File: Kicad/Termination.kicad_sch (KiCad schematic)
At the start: 27 parts, among them J1 Conn_02x25_Odd_Even, J5 5787170-5, SW1 219-8MST, U10 SN74F244DB, U8 DS21S07A, U9 DS21S07A

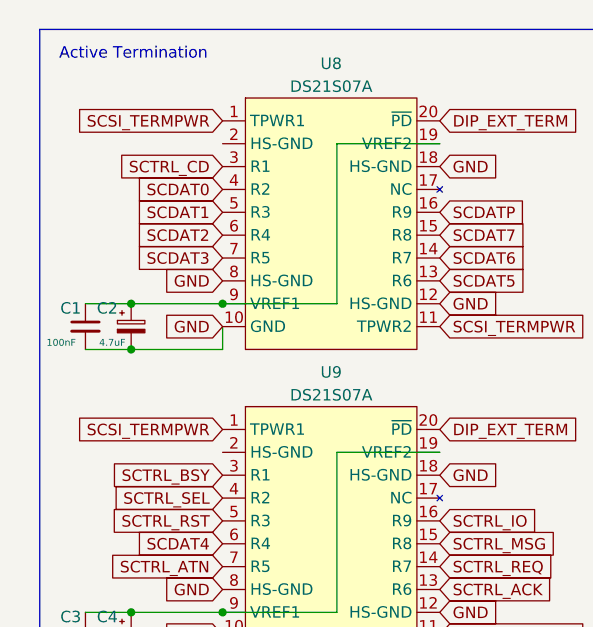
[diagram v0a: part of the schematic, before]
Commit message: Fix HS_GND connection on pin2 of the scsi terminators
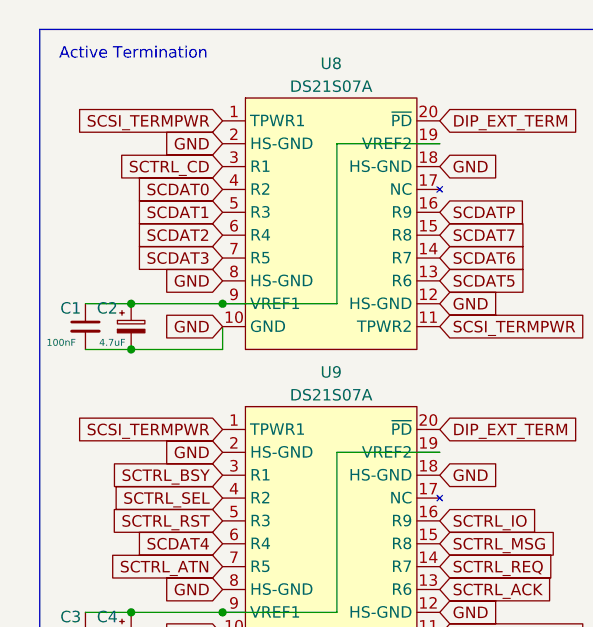
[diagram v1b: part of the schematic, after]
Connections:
- net GND: now also U8.2 (HS-GND), U9.2 (HS-GND)
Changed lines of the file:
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@@
+		)
+	)
+	(global_label "GND"
+		(shape input)
+		(at 36.83 62.23 180)
+		(fields_autoplaced yes)
+		(effects
+			(font
+				(size 1.27 1.27)
+			)
+			(justify right)
+		)
+		(property "Intersheetrefs" "${INTERSHEET_REFS}"
+			(at 29.9743 62.23 0)
+			(effects
+				(font
+					(size 1.27 1.27)
+				)
+				(justify right)
+				(hide yes)
+			)
 		)
 	)
@@
 			(effects
 				(font
+					(size 1.27 1.27)
+				)
+				(justify right)
+				(hide yes)
+			)
+		)
+	)
+	(global_label "GND"
+		(shape input)
+		(at 36.83 27.94 180)
+		(fields_autoplaced yes)
+		(effects
+			(font
+				(size 1.27 1.27)
+			)
+			(justify right)
+		)
+		(property "Intersheetrefs" "${INTERSHEET_REFS}"
+			(at 29.9743 27.94 0)
+			(effects
+				(font

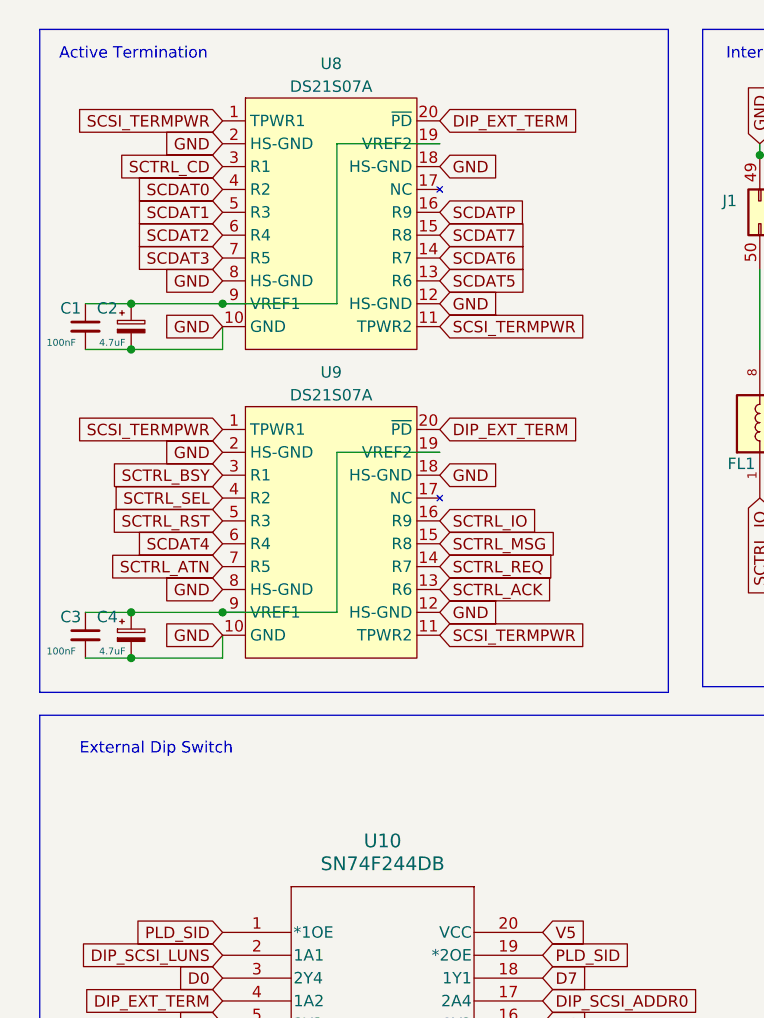
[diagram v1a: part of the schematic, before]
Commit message: Rename all Uxx parts from U1 to U13 for consistency
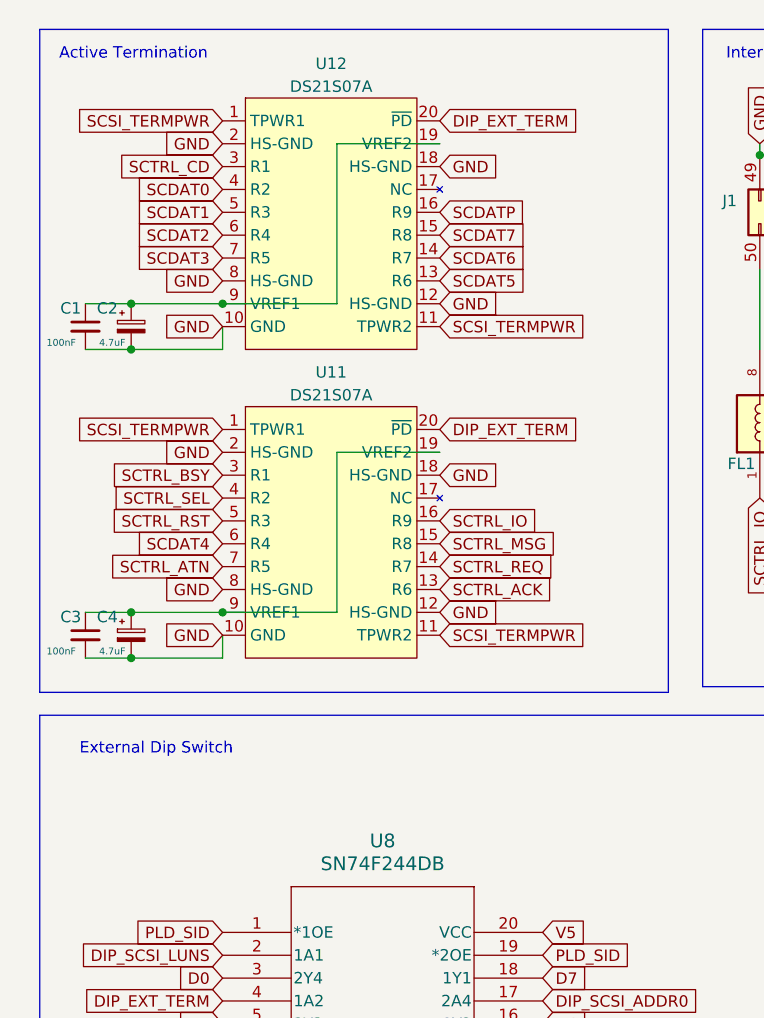
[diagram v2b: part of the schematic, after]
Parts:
- renumbered U9 to U11, U8 to U12, U10 to U8
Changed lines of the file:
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@@
 		(dnp no)
 		(fields_autoplaced yes)
-		(property "Reference" "U9"
+		(property "Reference" "U11"
 			(at 48.895 53.34 0)
 			(effects
@@
 			(project ""
 				(path "/8f9f4021-47aa-41d9-bea7-f6ccf72098bb/53e9e23b-3b92-4a87-a15c-9c224d6145c5"
-					(reference "U9")
+					(reference "U11")
 					(unit 1)
 				)
@@
 		(dnp no)
 		(fields_autoplaced yes)
-		(property "Reference" "U8"
+		(property "Reference" "U12"
 			(at 48.895 19.05 0)
 			(effects
@@
 			(project ""
 				(path "/8f9f4021-47aa-41d9-bea7-f6ccf72098bb/53e9e23b-3b92-4a87-a15c-9c224d6145c5"
-					(reference "U8")
+					(reference "U12")
 					(unit 1)
 				)
@@
 		(dnp no)
 		(fields_autoplaced yes)
-		(property "Reference" "U10"
+		(property "Reference" "U8"
 			(at 54.61 105.41 0)
 			(effects
@@
 			(project ""
 				(path "/8f9f4021-47aa-41d9-bea7-f6ccf72098bb/53e9e23b-3b92-4a87-a15c-9c224d6145c5"
-					(reference "U10")
+					(reference "U8")
 					(unit 1)
 				)

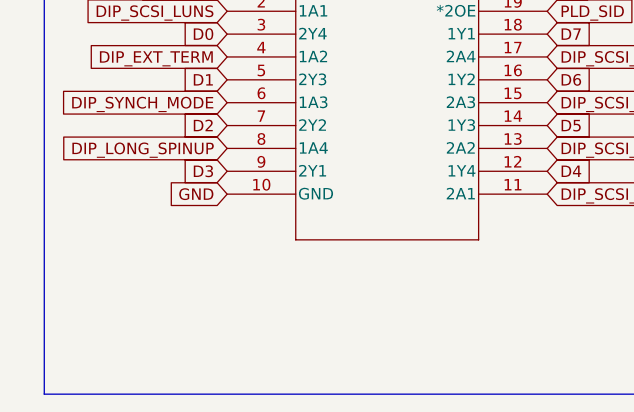
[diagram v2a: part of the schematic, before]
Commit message: Update sheet, add pull down on ROM_CE
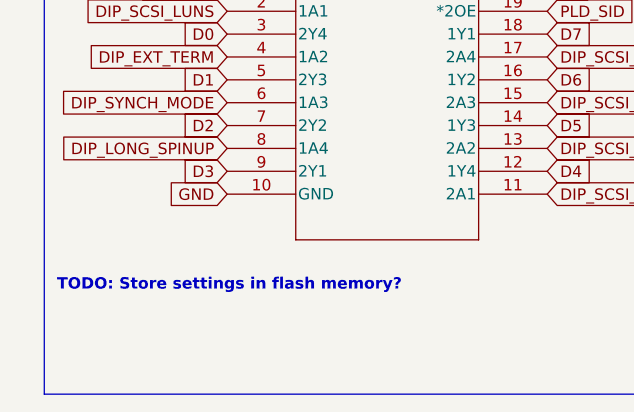
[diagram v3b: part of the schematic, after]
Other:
- note added: "TODO: Store settings in flash memory?"
- company: (none) -> amiga.technology
- title: (none) -> A4092
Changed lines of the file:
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@@
 	(generator_version "9.0")
 	(paper "A4")
+	(title_block
+		(title "A4092")
+		(rev "PROTO0")
+		(company "amiga.technology")
+	)
 	(rectangle
 		(start 90.17 15.24)
@@
 		)
 	)
+	(text "TODO: Store settings in flash memory?"
+		(exclude_from_sim no)
+		(at 37.084 148.59 0)
+		(effects
+			(font
+				(size 1.27 1.27)
+				(thickness 0.254)
+				(bold yes)
+			)
+		)
+	)

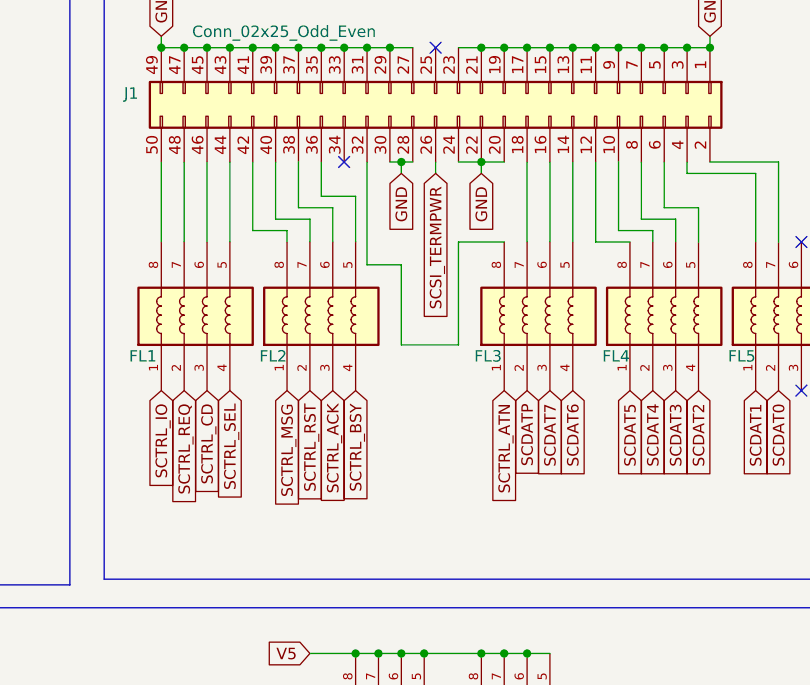
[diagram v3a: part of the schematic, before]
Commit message: Fix issues #12 and #13
Z_BEER and SCSI_BUSY were not connected correctly (single net pins)
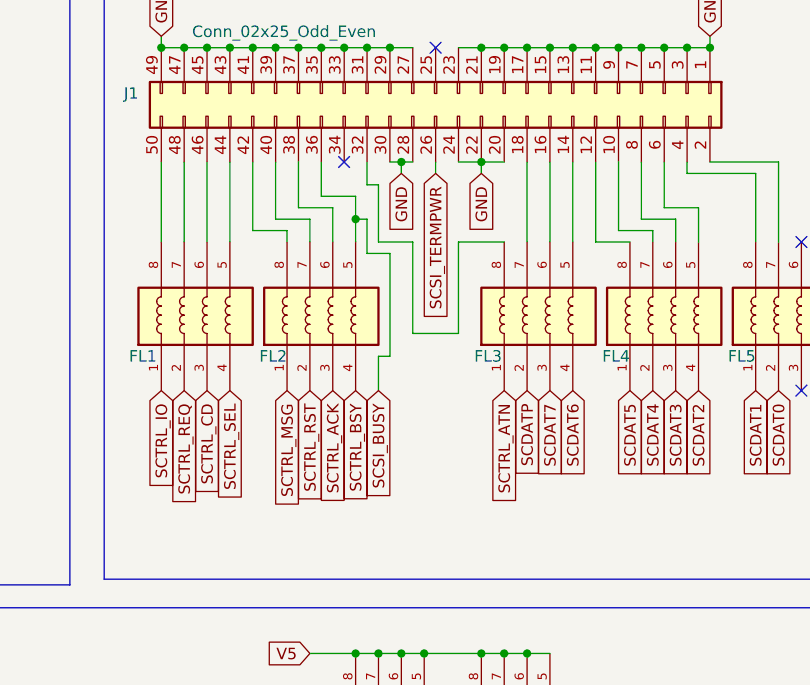
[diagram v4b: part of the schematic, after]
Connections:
- net SCSI_BUSY: now reaches FL2.5, J1.36 (Pin_36)
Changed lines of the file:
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@@
+	)
+	(junction
+		(at 118.11 48.26)
+		(diameter 0)
+		(color 0 0 0 0)
 	)
 	(junction
@@
 	(wire
 		(pts
+			(xy 118.11 48.26) (xy 118.11 50.8)
+		)
+		(stroke
+			(width 0)
+			(type default)
+		)
+	)
+	(wire
+		(pts
 			(xy 215.9 97.79) (xy 234.95 97.79)
 		)
@@
 	(wire
 		(pts
-			(xy 123.19 53.34) (xy 123.19 62.23)
+			(xy 124.46 50.8) (xy 124.46 60.96)
 		)
 		(stroke
@@
 	(wire
 		(pts
-			(xy 118.11 45.72) (xy 118.11 50.8)
+			(xy 118.11 45.72) (xy 118.11 48.26)
 		)
 		(stroke
@@
 	(wire
 		(pts
-			(xy 119.38 53.34) (xy 123.19 53.34)
-		)
-		(stroke
-			(width 0)
-			(type default)
-		)
-	)
-	(wire
-		(pts
 			(xy 234.95 64.77) (xy 234.95 66.04)
 		)
@@
 	(wire
 		(pts
-			(xy 129.54 62.23) (xy 129.54 50.8)
+			(xy 129.54 60.96) (xy 129.54 50.8)
 		)
 		(stroke
@@
 	(wire
 		(pts
+			(xy 120.65 50.8) (xy 124.46 50.8)
+		)
+		(stroke
+			(width 0)
+			(type default)
+		)
+	)
+	(wire
+		(pts
 			(xy 242.57 128.27) (xy 262.89 128.27)
 		)
@@
 	(wire
 		(pts
+			(xy 119.38 44.45) (xy 120.65 44.45)
+		)
+		(stroke
+			(width 0)
+			(type default)
+		)
+	)
+	(wire
+		(pts
 			(xy 116.84 29.21) (xy 119.38 29.21)
 		)
@@
 	(wire
 		(pts
+			(xy 118.11 48.26) (xy 119.38 48.26)
+		)
+		(stroke
+			(width 0)
+			(type default)
+		)
+	)
+	(wire
+		(pts
 			(xy 215.9 144.78) (xy 217.17 144.78)
 		)
@@
 	(wire
 		(pts
+			(xy 121.92 63.5) (xy 121.92 52.07)
+		)
+		(stroke
+			(width 0)
+			(type default)
+		)
+	)
+	(wire
+		(pts
 			(xy 99.06 41.91) (xy 99.06 50.8)
 		)
@@
 	(wire
 		(pts
+			(xy 120.65 67.31) (xy 120.65 63.5)
+		)
+		(stroke
+			(width 0)
+			(type default)
+		)
+	)
+	(wire
+		(pts
 			(xy 257.81 54.61) (xy 262.89 54.61)
 		)
@@
 	(wire
 		(pts
+			(xy 119.38 48.26) (xy 119.38 52.07)
+		)
+		(stroke
+			(width 0)
+			(type default)
+		)
+	)
+	(wire
+		(pts
 			(xy 262.89 34.29) (xy 262.89 36.83)
 		)
@@
 	(wire
 		(pts
+			(xy 119.38 52.07) (xy 121.92 52.07)
+		)
+		(stroke
+			(width 0)
+			(type default)
+		)
+	)
+	(wire
+		(pts
 			(xy 101.6 29.21) (xy 104.14 29.21)
 		)
@@
 	(wire
 		(pts
-			(xy 119.38 41.91) (xy 119.38 53.34)
+			(xy 119.38 41.91) (xy 119.38 44.45)
 		)
 		(stroke
@@
 	(wire
 		(pts
+			(xy 120.65 63.5) (xy 121.92 63.5)
+		)
+		(stroke
+			(width 0)
+			(type default)
+		)
+	)
+	(wire
+		(pts
+			(xy 120.65 44.45) (xy 120.65 50.8)
+		)
+		(stroke
+			(width 0)
+			(type default)
+		)
+	)
+	(wire
+		(pts
 			(xy 118.11 116.84) (xy 118.11 123.19)
 		)
@@
 	(wire
 		(pts
-			(xy 123.19 62.23) (xy 129.54 62.23)
+			(xy 124.46 60.96) (xy 129.54 60.96)
 		)
 		(stroke
@@
 		)
 	)
+	(global_label "SCSI_BUSY"
+		(shape input)
+		(at 120.65 67.31 270)
+		(fields_autoplaced yes)
+		(effects
+			(font
+				(size 1.27 1.27)
+			)
+			(justify right)
+		)
+		(property "Intersheetrefs" "${INTERSHEET_REFS}"
+			(at 120.65 80.4552 90)
+			(effects
+				(font
+					(size 1.27 1.27)
+				)
+				(justify right)
+				(hide yes)
+			)
+		)
+	)

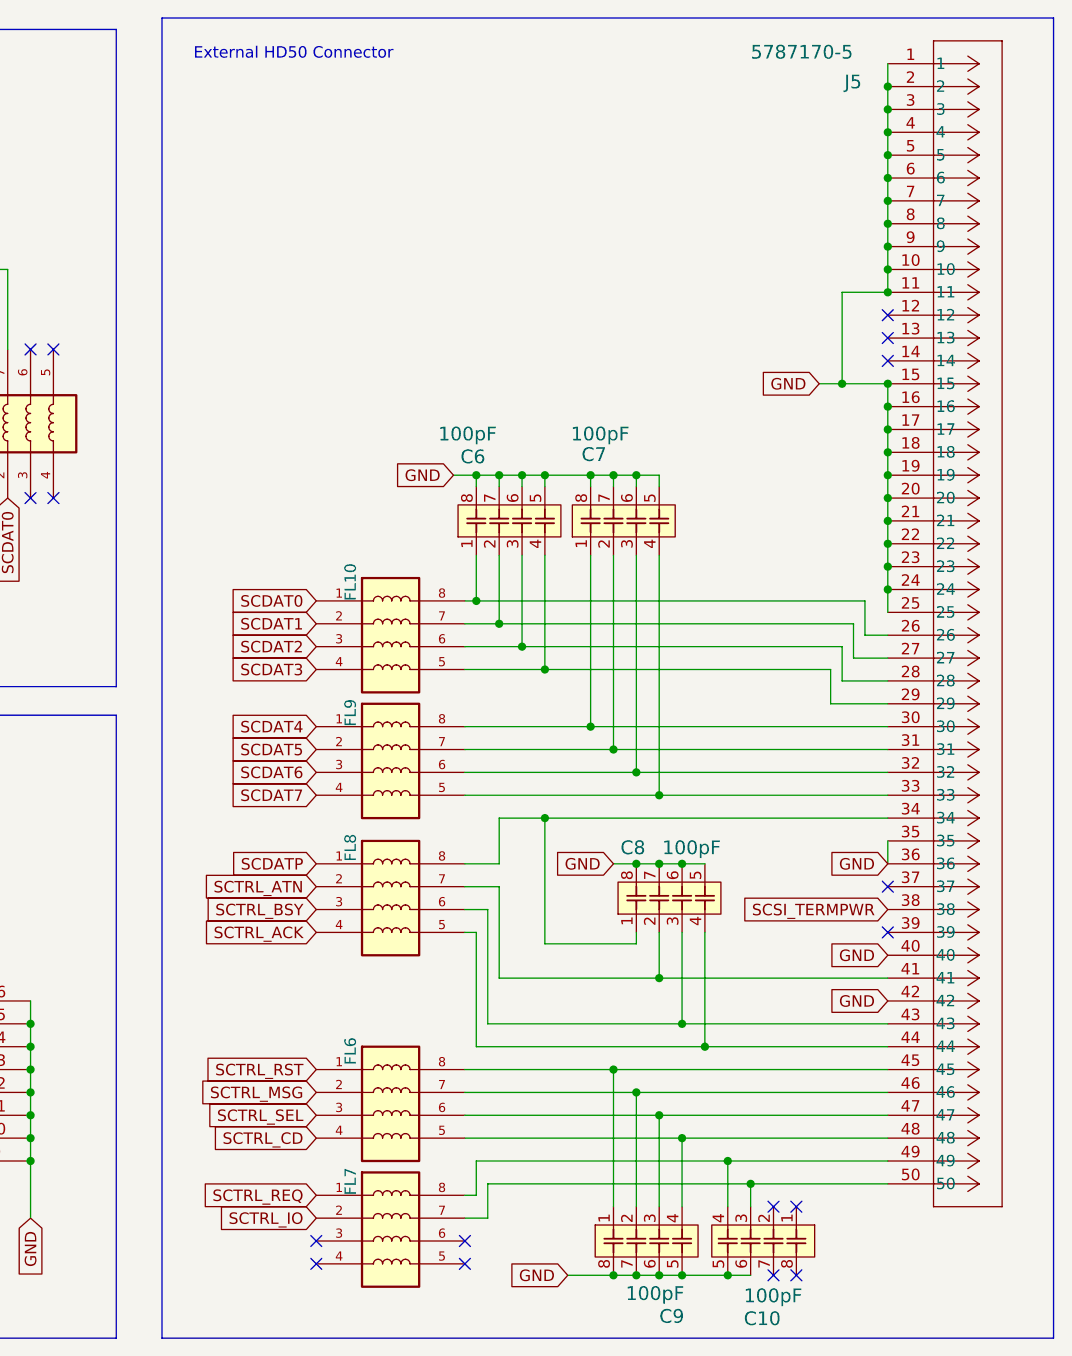
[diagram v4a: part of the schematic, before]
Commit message: Move HPDB50 connector to back panel
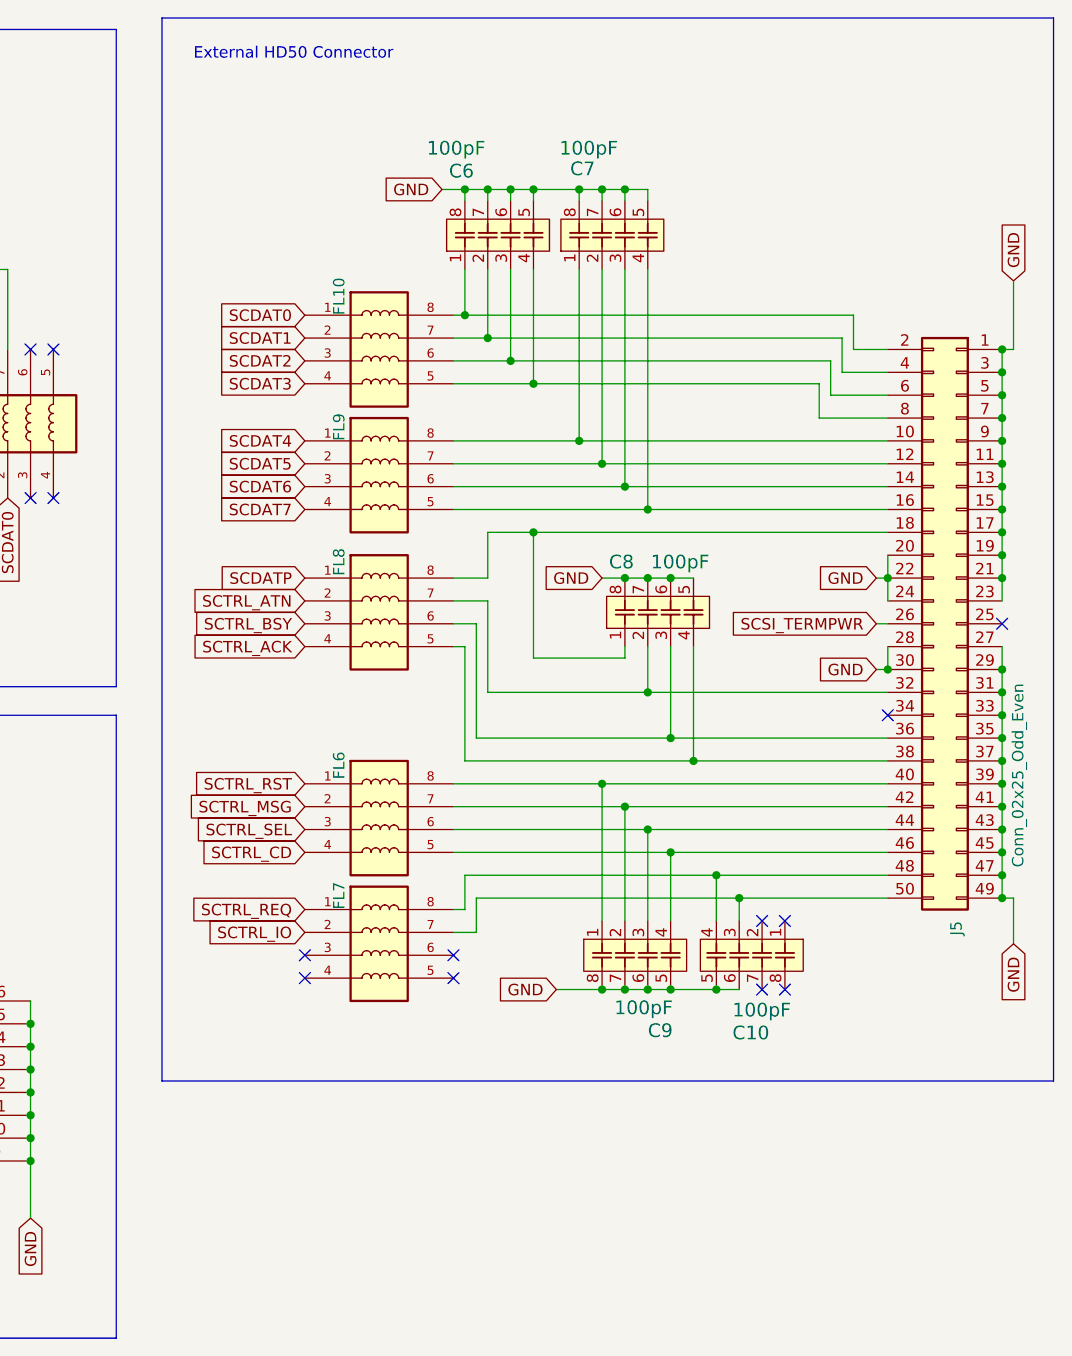
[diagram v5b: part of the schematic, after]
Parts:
- removed J5: 5787170-5, 5787170_5:CONN_5787170-5_TYC, symbol 5787170_5:5787170-5
- added J5: Conn_02x25_Odd_Even, kicad-official/Connector_IDC.pretty:IDC-Header_2x25_P2.54mm_Vertical, symbol Connector_Generic:Conn_02x25_Odd_Even
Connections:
- net GND: now also J5.1 (Pin_1), J5.11 (Pin_11), J5.13 (Pin_13), J5.15 (Pin_15), J5.17 (Pin_17), J5.19 (Pin_19), J5.20 (Pin_20), J5.21 (Pin_21), J5.22 (Pin_22), J5.23 (Pin_23), J5.24 (Pin_24), J5.27 (Pin_27), J5.28 (Pin_28), J5.29 (Pin_29), J5.3 (Pin_3), J5.30 (Pin_30), J5.31 (Pin_31), J5.33 (Pin_33), J5.35 (Pin_35), J5.37 (Pin_37), J5.39 (Pin_39), J5.41 (Pin_41), J5.43 (Pin_43), J5.45 (Pin_45), J5.47 (Pin_47), J5.49 (Pin_49), J5.5 (Pin_5), J5.7 (Pin_7), J5.9 (Pin_9)
- net SCSI_TERMPWR: now also J5.26 (Pin_26)
- net at C8.4, FL8.5: now also J5.38 (Pin_38)
- net at C8.3, FL8.6: now also J5.36 (Pin_36)
- net at C8.2, FL8.7: now also J5.32 (Pin_32)
- net at C8.1, FL8.8: now also J5.18 (Pin_18)
- net at C6.1, FL10.8: now also J5.2 (Pin_2)
- net at C6.2, FL10.7: now also J5.4 (Pin_4)
- net at C6.3, FL10.6: now also J5.6 (Pin_6)
- net at C6.4, FL10.5: now also J5.8 (Pin_8)
- net at C7.1, FL9.8: now also J5.10 (Pin_10)
- net at C7.2, FL9.7: now also J5.12 (Pin_12)
- net at C7.3, FL9.6: now also J5.14 (Pin_14)
- net at C7.4, FL9.5: now also J5.16 (Pin_16)
- net at C9.1, FL6.8: now also J5.40 (Pin_40)
- net at C9.2, FL6.7: now also J5.42 (Pin_42)
- net at C9.3, FL6.6: now also J5.44 (Pin_44)
- net at C9.4, FL6.5: now also J5.46 (Pin_46)
- net at C10.4, FL7.8: now also J5.48 (Pin_48)
- net at C10.3, FL7.7: now also J5.50 (Pin_50)
- no-connect marks 19 -> 16
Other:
- moved on the sheet: C10, C6, C7, C8, C9, FL10, FL6, FL7, FL8, FL9
